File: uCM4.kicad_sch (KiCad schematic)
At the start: 2 parts

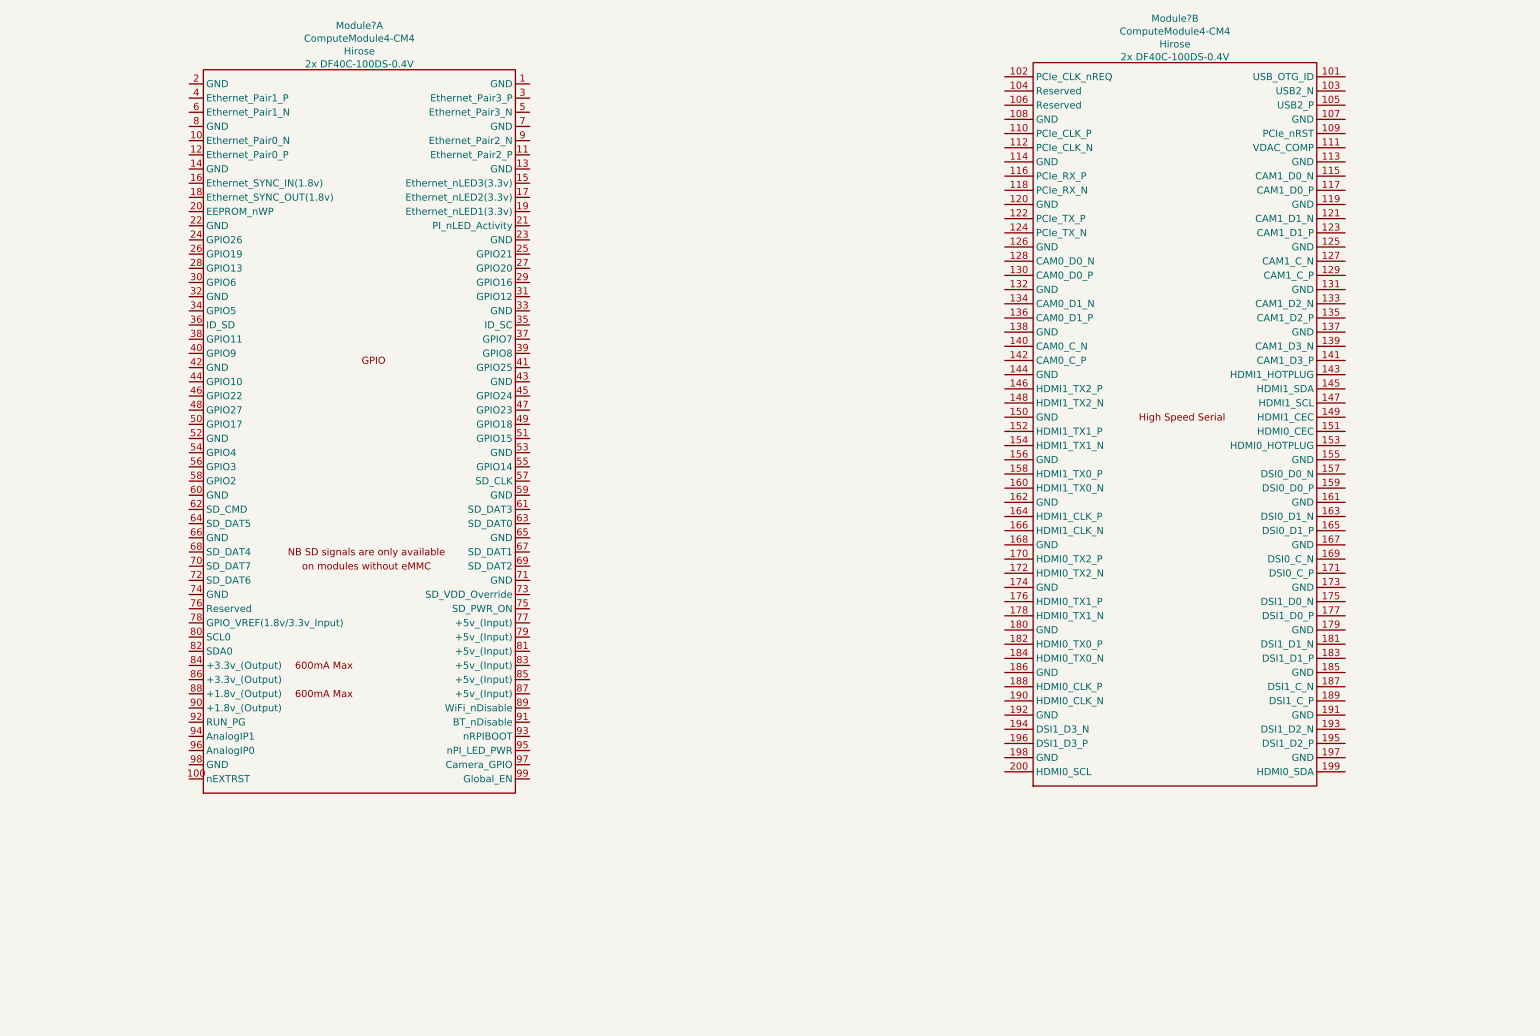
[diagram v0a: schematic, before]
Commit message: Add schematics
Implement most of the schematics part of the project. What is left are
less important details, like power button and LEDs. All such cases, no
matter the reason, are marked with TODO.
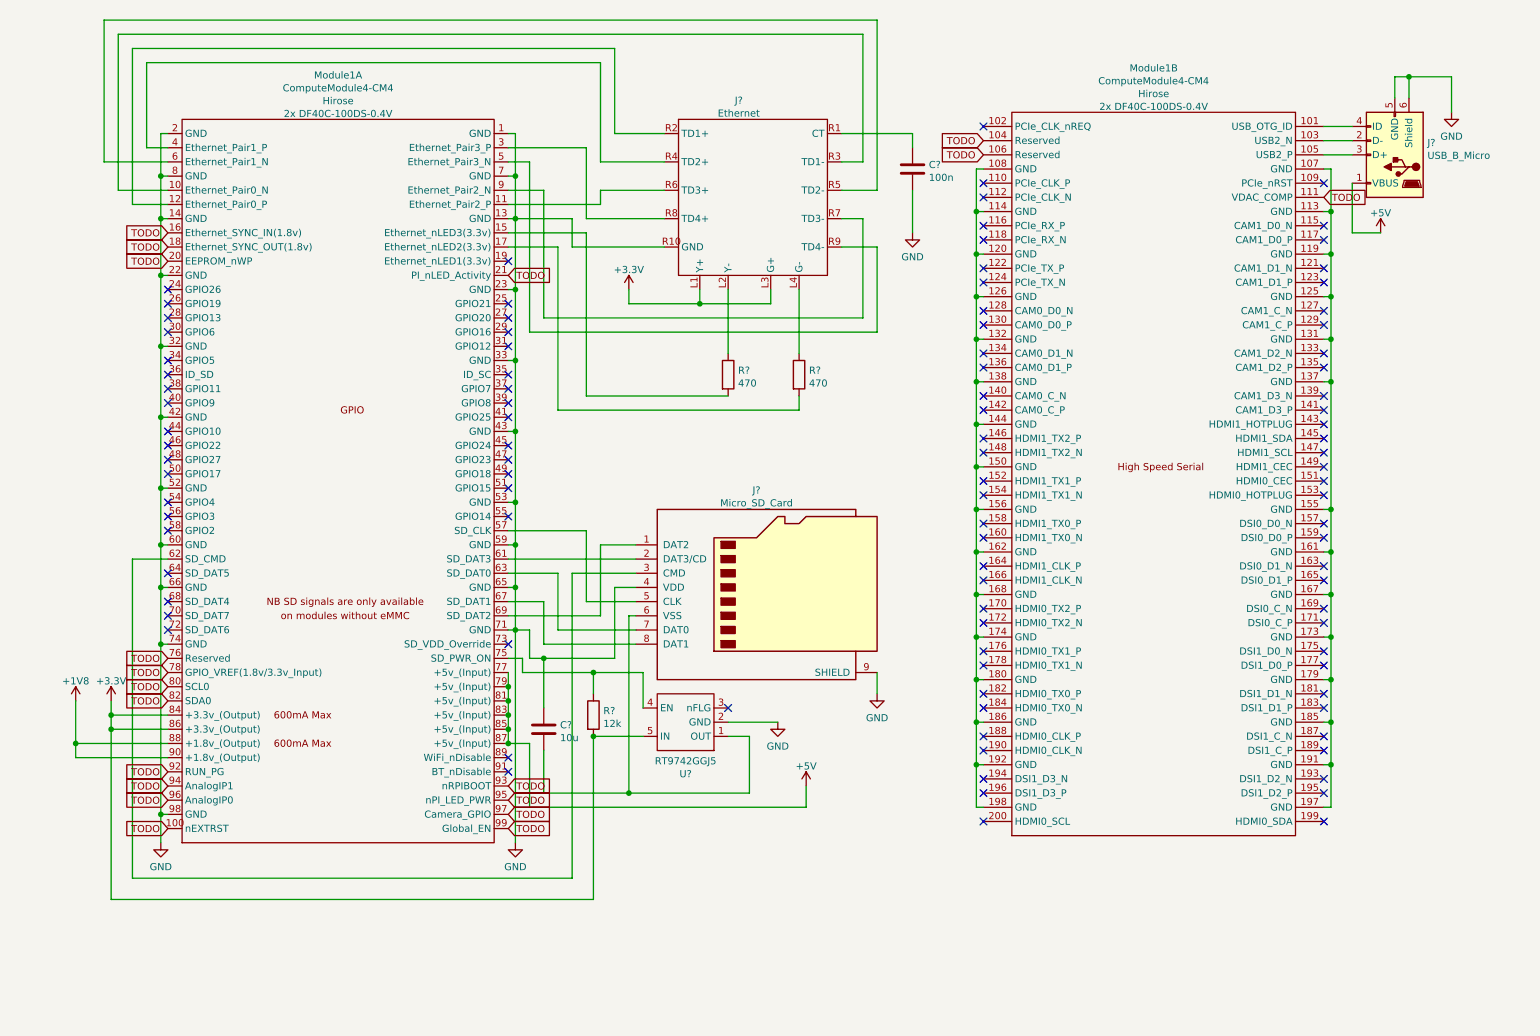
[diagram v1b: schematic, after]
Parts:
- added C?: 10u, symbol Device:C
- added C?: 100n, symbol Device:C
- added J?: Ethernet, symbol Special:Ethernet
- added J?: USB_B_Micro, symbol Connector:USB_B_Micro
- added J?: Micro_SD_Card, symbol Connector:Micro_SD_Card
- added R?: 12k, symbol Device:R
- added R? (x2): 470, symbol Device:R
- added U?: RT9742GGJ5, Package_TO_SOT_SMD:SOT-23-5, symbol CM4IO:RT9742GGJ5
- gave numbers to parts that had none: 1
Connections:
- net at Module1.101 (USB_OTG_ID): now also J?.4 (ID)
- net at Module1.103 (USB2_N): now also J?.2 (D-)
- net TODO: now reaches Module1.104 (Reserved)
- net TODO: now also Module1.100 (nEXTRST), Module1.106 (Reserved), Module1.111 (VDAC_COMP), Module1.16 (Ethernet_SYNC_IN(1.8v)), Module1.18 (Ethernet_SYNC_OUT(1.8v)), Module1.20 (EEPROM_nWP), Module1.21 (PI_nLED_Activity), Module1.76 (Reserved), Module1.78 (GPIO_VREF(1.8v/3.3v_Input)), Module1.80 (SCL0), Module1.82 (SDA0), Module1.92 (RUN_PG), Module1.93 (nRPIBOOT), Module1.94 (AnalogIP1), Module1.95 (nPI_LED_PWR), Module1.96 (AnalogIP0), Module1.97 (Camera_GPIO), Module1.99 (Global_EN)
- net at Module1.105 (USB2_P): now also J?.3 (D+)
- net at Module1.107 (GND): now also Module1.113 (GND), Module1.119 (GND), Module1.125 (GND), Module1.131 (GND), Module1.137 (GND), Module1.155 (GND), Module1.161 (GND), Module1.167 (GND), Module1.173 (GND), Module1.179 (GND), Module1.185 (GND), Module1.191 (GND), Module1.197 (GND)
- net at Module1.108 (GND): now also Module1.114 (GND), Module1.120 (GND), Module1.126 (GND), Module1.132 (GND), Module1.138 (GND), Module1.144 (GND), Module1.150 (GND), Module1.156 (GND), Module1.162 (GND), Module1.168 (GND), Module1.174 (GND), Module1.180 (GND), Module1.186 (GND), Module1.192 (GND), Module1.198 (GND)
- net GND: now reaches Module1.1 (GND)
- net GND: now also Module1.13 (GND), Module1.14 (GND), Module1.2 (GND), Module1.22 (GND), Module1.23 (GND), Module1.32 (GND), Module1.33 (GND), Module1.42 (GND), Module1.43 (GND), Module1.52 (GND), Module1.53 (GND), Module1.59 (GND), Module1.60 (GND), Module1.65 (GND), Module1.66 (GND), Module1.7 (GND), Module1.71 (GND), Module1.74 (GND), Module1.8 (GND), Module1.98 (GND), C?.1, C?.2, J?.4 (VDD), J?.5 (GND), J?.6 (Shield), J?.9 (SHIELD), J?.R10 (GND), U?.2 (GND)
- net at Module1.10 (Ethernet_Pair0_N): now also J?.R3 (TD1-)
- net at Module1.11 (Ethernet_Pair2_P): now also J?.R6 (TD3+)
- net at Module1.12 (Ethernet_Pair0_P): now also J?.R2 (TD1+)
- net at Module1.15 (Ethernet_nLED3(3.3v)): now also R?.2
- net at Module1.17 (Ethernet_nLED2(3.3v)): now also R?.2
- net at Module1.3 (Ethernet_Pair3_P): now also J?.R8 (TD4+)
- net at Module1.4 (Ethernet_Pair1_P): now also J?.R4 (TD2+)
- net at Module1.5 (Ethernet_Pair3_N): now also J?.R9 (TD4-)
- net at Module1.57 (SD_CLK): now also J?.5 (CLK)
- net at Module1.6 (Ethernet_Pair1_N): now also J?.R5 (TD2-)
- net at Module1.61 (SD_DAT3): now also J?.2 (DAT3/CD)
- net at Module1.62 (SD_CMD): now also J?.3 (CMD)
- net at Module1.63 (SD_DAT0): now also J?.7 (DAT0)
- net at Module1.67 (SD_DAT1): now also J?.8 (DAT1)
- net at Module1.69 (SD_DAT2): now also J?.1 (DAT2)
- net at Module1.75 (SD_PWR_ON): now also R?.1, U?.4 (EN)
- net +5V: now reaches Module1.77 (+5v_(Input))
- net +5V: now also Module1.79 (+5v_(Input)), Module1.81 (+5v_(Input)), Module1.83 (+5v_(Input)), Module1.85 (+5v_(Input)), Module1.87 (+5v_(Input)), J?.1 (VBUS)
- net +3V3: now reaches Module1.84 (+3.3v_(Output))
- net +3V3: now also Module1.86 (+3.3v_(Output)), J?.L1 (Y+), J?.L3 (G+), R?.2, U?.5 (IN)
- net +1V8: now reaches Module1.88 (+1.8v_(Output))
- net +1V8: now also Module1.90 (+1.8v_(Output))
- net at Module1.9 (Ethernet_Pair2_N): now also J?.R7 (TD3-)
- new net: J?.L2 (Y-), R?.1
- new net: J?.L4 (G-), R?.1
- new net: C?.1, J?.R1 (CT)
- new net: C?.2, J?.6 (VSS), U?.1 (OUT)
- no-connect marks 0 -> 101
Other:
- title: (none) -> uCM4 Daughter Board
- moved on the sheet: Module1A, Module1B

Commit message: Implement missing parts of schematics
Add LEDs, ESD protection on USB connector and mark some pins as unused.

What is left for considerations is implementing RTC. Maybe Ethernet has
to be converted to bus, as wires within a pair has to be same length.
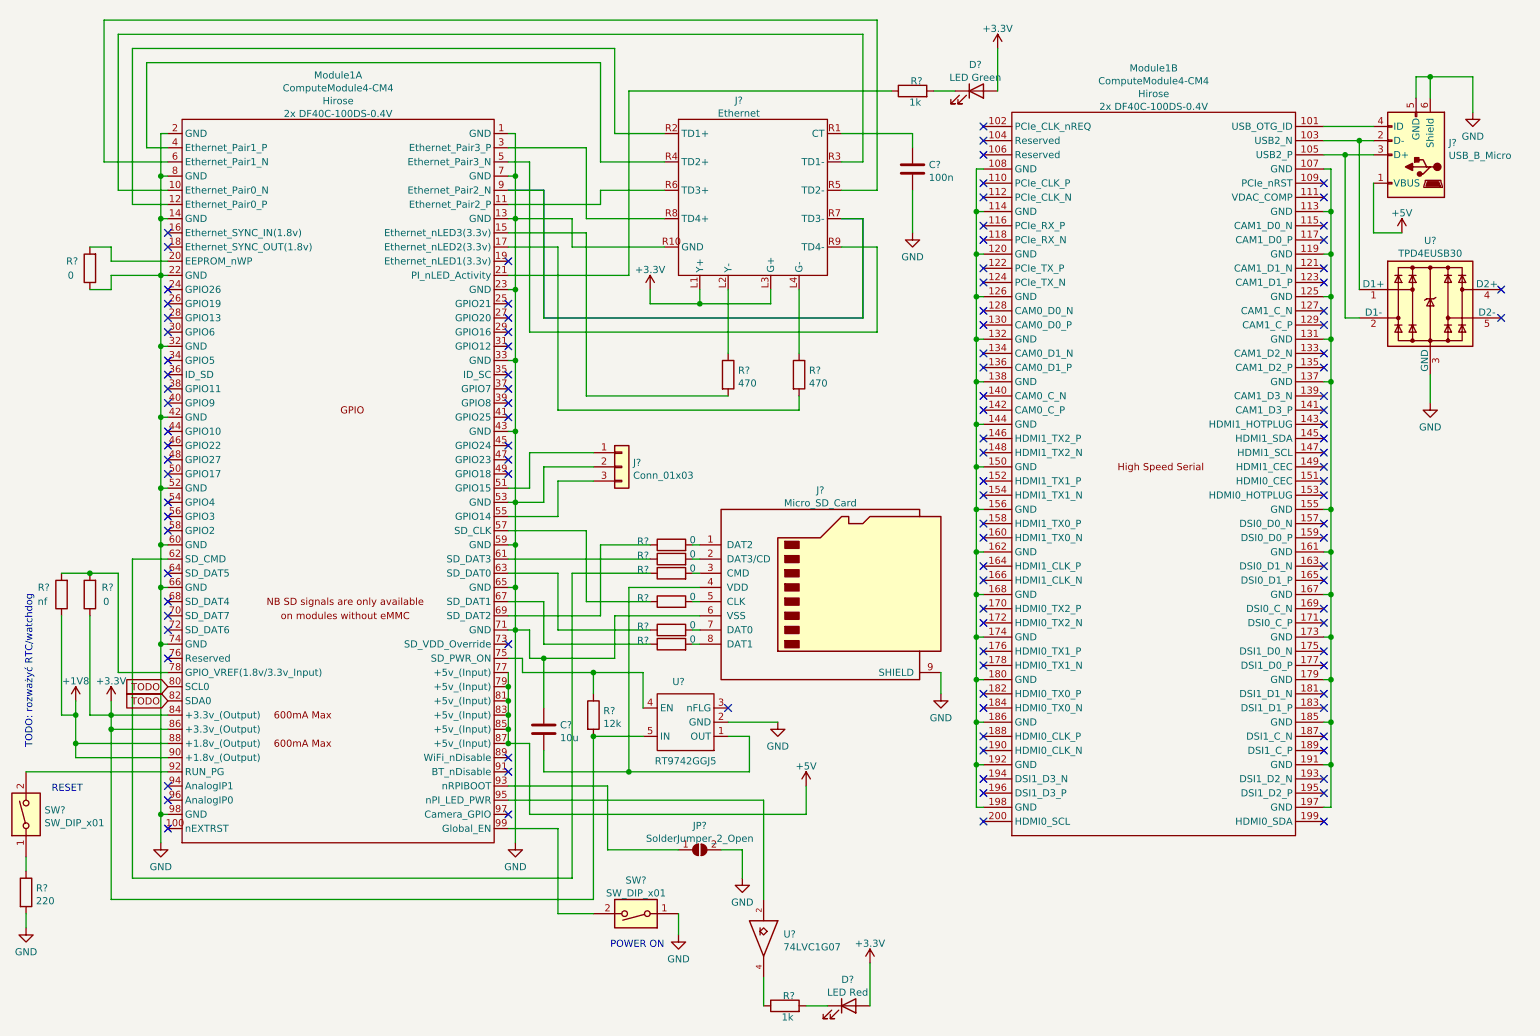
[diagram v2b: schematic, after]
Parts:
- added D?: LED Red, symbol Device:LED
- added D?: LED Green, symbol Device:LED
- added J?: Conn_01x03, symbol Connector_Generic:Conn_01x03
- added JP?: SolderJumper_2_Open, symbol Jumper:SolderJumper_2_Open
- added R?: 220, symbol Device:R
- added R? (x8): 0, symbol Device:R
- added R? (x2): 1k, symbol Device:R
- added R?: nf, symbol Device:R
- added SW? (x2): SW_DIP_x01, symbol Switch:SW_DIP_x01
- added U?: TPD4EUSB30, Package_SON:USON-10_2.5x1.0mm_P0.5mm, symbol Power_Protection:TPD4EUSB30
- added U?: 74LVC1G07, symbol 74xGxx:74LVC1G07
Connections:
- net +1V8: now also R?.1
- net +3V3: now also D?.2 (A), D?.2 (A), R?.1
- net GND: now also J?.6 (VSS), J?.2 (Pin_2), JP?.2 (B), R?.1, R?.2, SW?.1, U?.3 (GND), U?.3 (GND), U?.8 (GND); no longer J?.4 (VDD)
- net TODO: no longer Module1.100 (nEXTRST), Module1.104 (Reserved), Module1.106 (Reserved), Module1.111 (VDAC_COMP), Module1.16 (Ethernet_SYNC_IN(1.8v)), Module1.18 (Ethernet_SYNC_OUT(1.8v)), Module1.20 (EEPROM_nWP), Module1.21 (PI_nLED_Activity), Module1.76 (Reserved), Module1.78 (GPIO_VREF(1.8v/3.3v_Input)), Module1.92 (RUN_PG), Module1.93 (nRPIBOOT), Module1.94 (AnalogIP1), Module1.95 (nPI_LED_PWR), Module1.96 (AnalogIP0), Module1.97 (Camera_GPIO), Module1.99 (Global_EN)
- net at J?.2 (D-), Module1.103 (USB2_N): now also U?.1 (D1+)
- net at J?.3 (D+), Module1.105 (USB2_P): now also U?.2 (D1-)
- net at Module1.51 (GPIO15): now also J?.1 (Pin_1)
- net at Module1.55 (GPIO14): now also J?.3 (Pin_3)
- net at Module1.57 (SD_CLK): now also R?.1; no longer J?.5 (CLK)
- net at Module1.61 (SD_DAT3): now also R?.1; no longer J?.2 (DAT3/CD)
- net at Module1.62 (SD_CMD): now also R?.1; no longer J?.3 (CMD)
- net at Module1.63 (SD_DAT0): now also R?.1; no longer J?.7 (DAT0)
- net at Module1.67 (SD_DAT1): now also R?.1; no longer J?.8 (DAT1)
- net at Module1.69 (SD_DAT2): now also R?.1; no longer J?.1 (DAT2)
- net at C?.2, U?.1 (OUT): now also J?.4 (VDD); no longer J?.6 (VSS)
- new net: D?.1 (K), R?.2 (x2)
- new net: Module1.95 (nPI_LED_PWR), U?.2
- new net: R?.1, U?.4
- new net: R?.1, SW?.1
- new net: Module1.99 (Global_EN), SW?.2
- new net: Module1.92 (RUN_PG), SW?.2
- new net: J?.8 (DAT1), R?.2
- new net: J?.5 (CLK), R?.2
- new net: J?.7 (DAT0), R?.2
- new net: J?.2 (DAT3/CD), R?.2
- new net: Module1.20 (EEPROM_nWP), R?.2
- new net: Module1.21 (PI_nLED_Activity), R?.1
- new net: Module1.78 (GPIO_VREF(1.8v/3.3v_Input)), R?.2, R?.2
- new net: JP?.1 (A), Module1.93 (nRPIBOOT)
- new net: J?.3 (CMD), R?.2
- new net: J?.1 (DAT2), R?.2
- new net VCC: U?.5 (VCC)
- no-connect marks 101 -> 111
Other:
- note added: "POWER ON"
- note added: "RESET"
- note added: "TODO: rozważyć RTC/watchdog"
- title: uCM4 Daughter Board -> uCM4 Base Board
- moved on the sheet: J?

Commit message: Populate PCB
Almost all footprints ready. Missing is, most importantly, MicroUSB
connector.
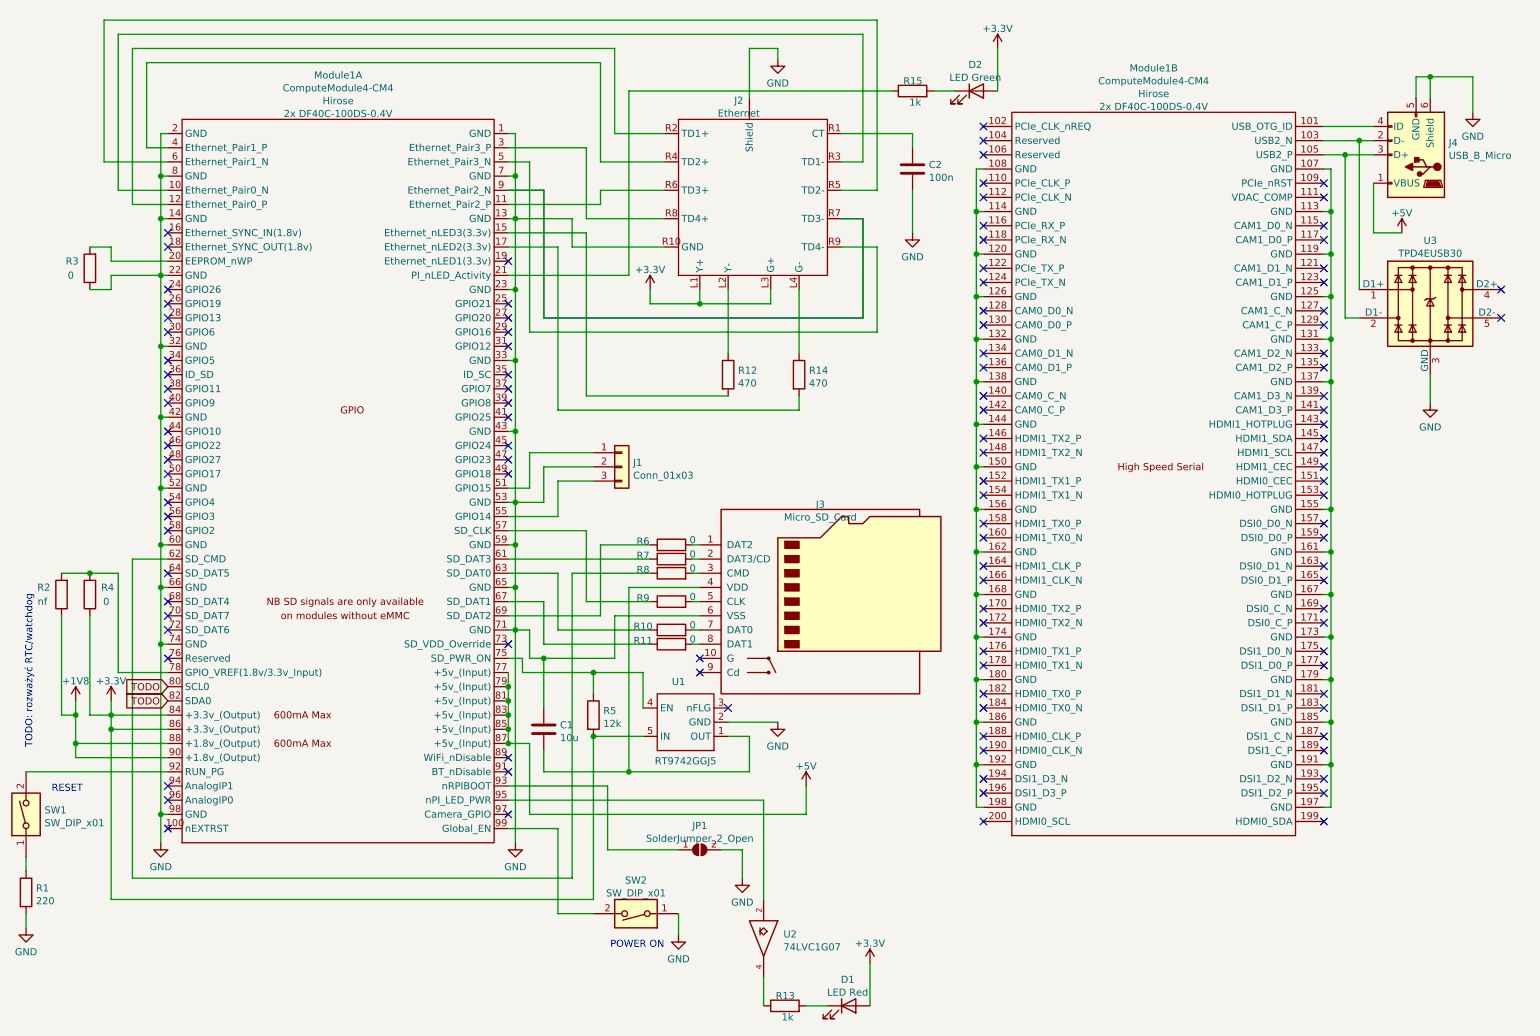
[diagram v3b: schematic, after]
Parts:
- C1, C2: renamed from C?; footprint (none) -> Capacitor_SMD:C_0603_1608Metric_Pad1.08x0.95mm_HandSolder
- D1, D2: renamed from D?; footprint (none) -> LED_SMD:LED_0603_1608Metric_Pad1.05x0.95mm_HandSolder
- J1: renamed from J?; footprint (none) -> Connector_PinHeader_2.54mm:PinHeader_1x03_P2.54mm_Vertical
- J2: renamed from J?; footprint (none) -> Connector_RJ:RJ45_UDE_RB1-125B8G1A
- J3: renamed from J?; footprint (none) -> Special:TF-015; symbol Connector:Micro_SD_Card -> Special:Micro_SD_Card_Det
- R1, R12, R13, R14, R15, R2, R3, R4, R5: renamed from R?; footprint (none) -> Resistor_SMD:R_0603_1608Metric_Pad0.98x0.95mm_HandSolder
- R10, R11, R6, R7, R8, R9: renamed from R?; footprint (none) -> Resistor_SMD:R_0402_1005Metric_Pad0.72x0.64mm_HandSolder
- U2: renamed from U?; footprint (none) -> Package_TO_SOT_SMD:SOT-353_SC-70-5_Handsoldering
- gave numbers to parts that had none: 6
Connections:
- net GND: now also J2. (Shield); no longer J3.9 (SHIELD)
- no-connect marks 111 -> 113

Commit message: Add MicroUSB connector
Unfinished, but functional.
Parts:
- J4: footprint (none) -> Special:U254-05XX-4BH83
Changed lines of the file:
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@@
       (effects (font (size 1.27 1.27)) (justify right))
     )
-    (property "Footprint" "" (id 2) (at 261.62 40.64 0)
+    (property "Footprint" "Special:U254-05XX-4BH83" (id 2) (at 261.62 40.64 0)
       (effects (font (size 1.27 1.27)) hide)
     )
@@
     )
     (path "/37290dec-d4dd-4c56-8b24-17283c9726cb"
-      (reference "J4") (unit 1) (value "USB_B_Micro") (footprint "")
+      (reference "J4") (unit 1) (value "USB_B_Micro") (footprint "Special:U254-05XX-4BH83")
     )
     (path "/debd560e-0565-4cbf-9569-5f25352bd66e"
